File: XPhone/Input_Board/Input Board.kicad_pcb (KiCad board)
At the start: 2 copper layers, 92 parts, among them J1 AUDIO, J10 ENV, J11 PULSE, J12 PULSE, J2 AUDIO, J3 ENV, J4 ENV, J5 PULSE, J6 PULSE, J7 AUDIO, J8 AUDIO, J9 ENV, Q1 BC847CW, Q2 BC847CW, Q3 BC847CW, Q4 BC847CW, Q5 BC847CW, Q6 BC847CW, Q7 BC847CW, Q8 BC847CW, U1 LM833, U2 78L05, U3 TL084, U4 74HC14, U5 LM833

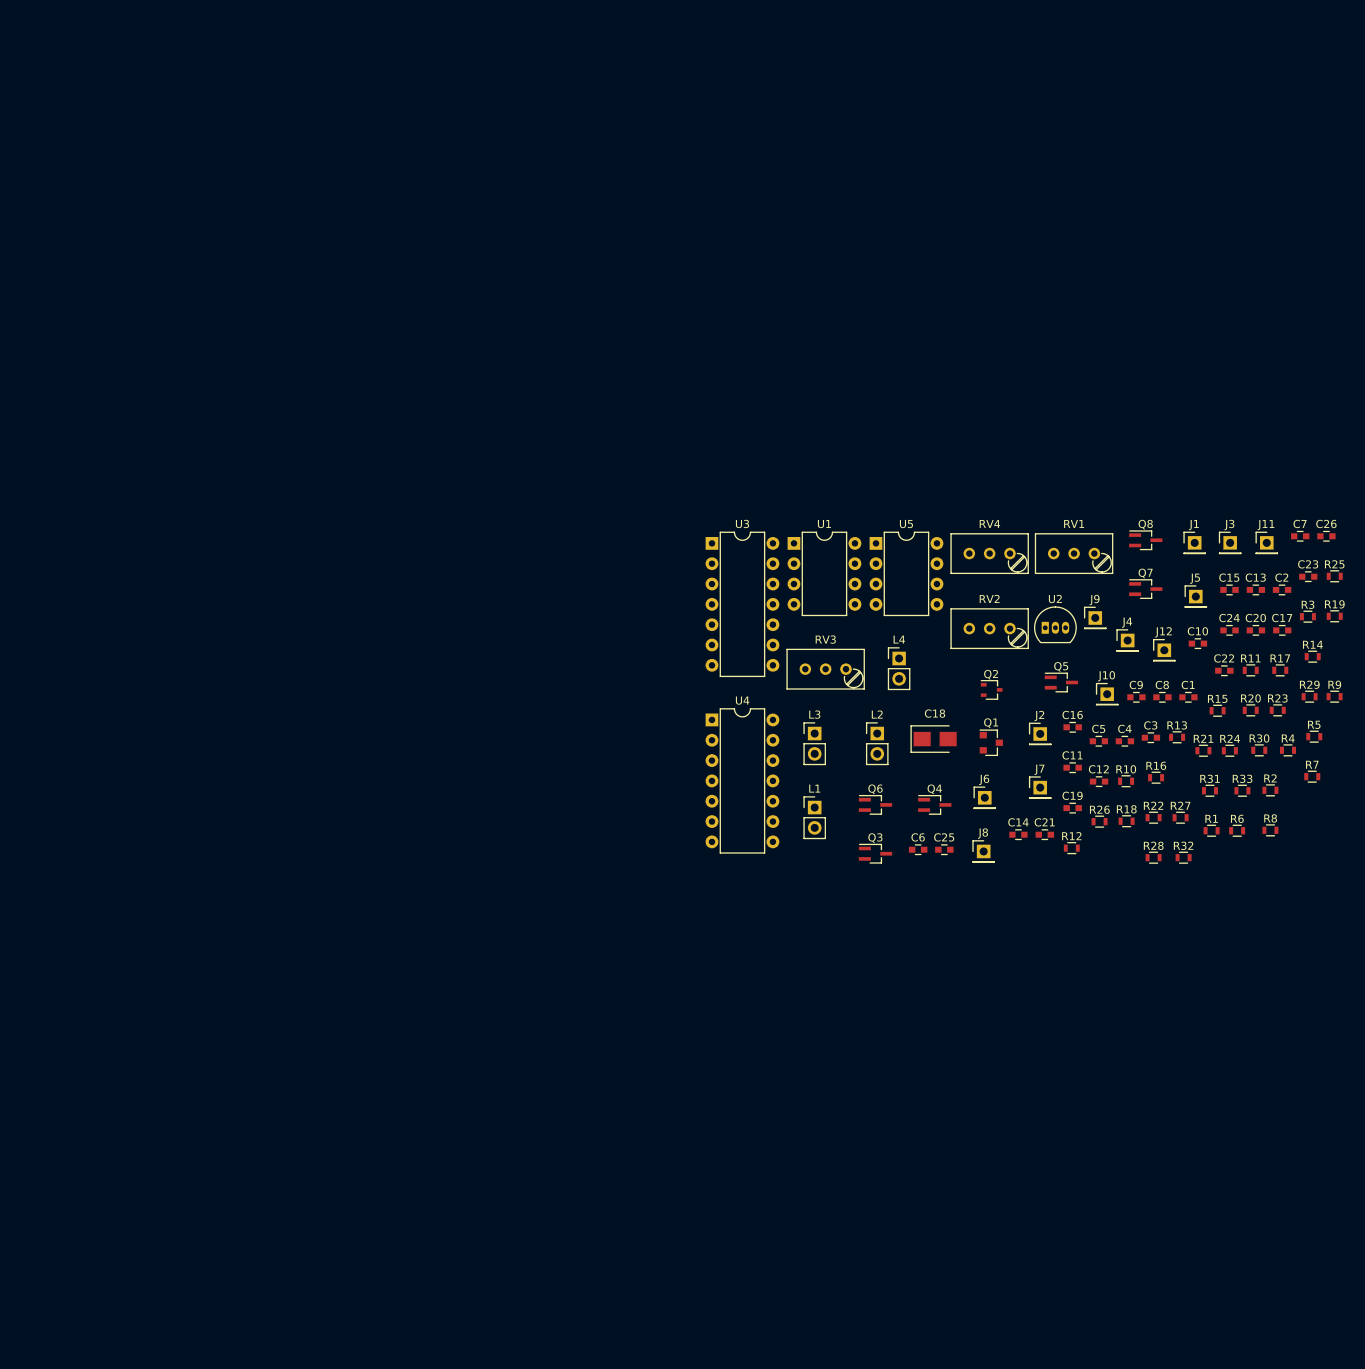
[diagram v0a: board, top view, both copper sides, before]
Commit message: ^XPhone Input Board layout; +bug record
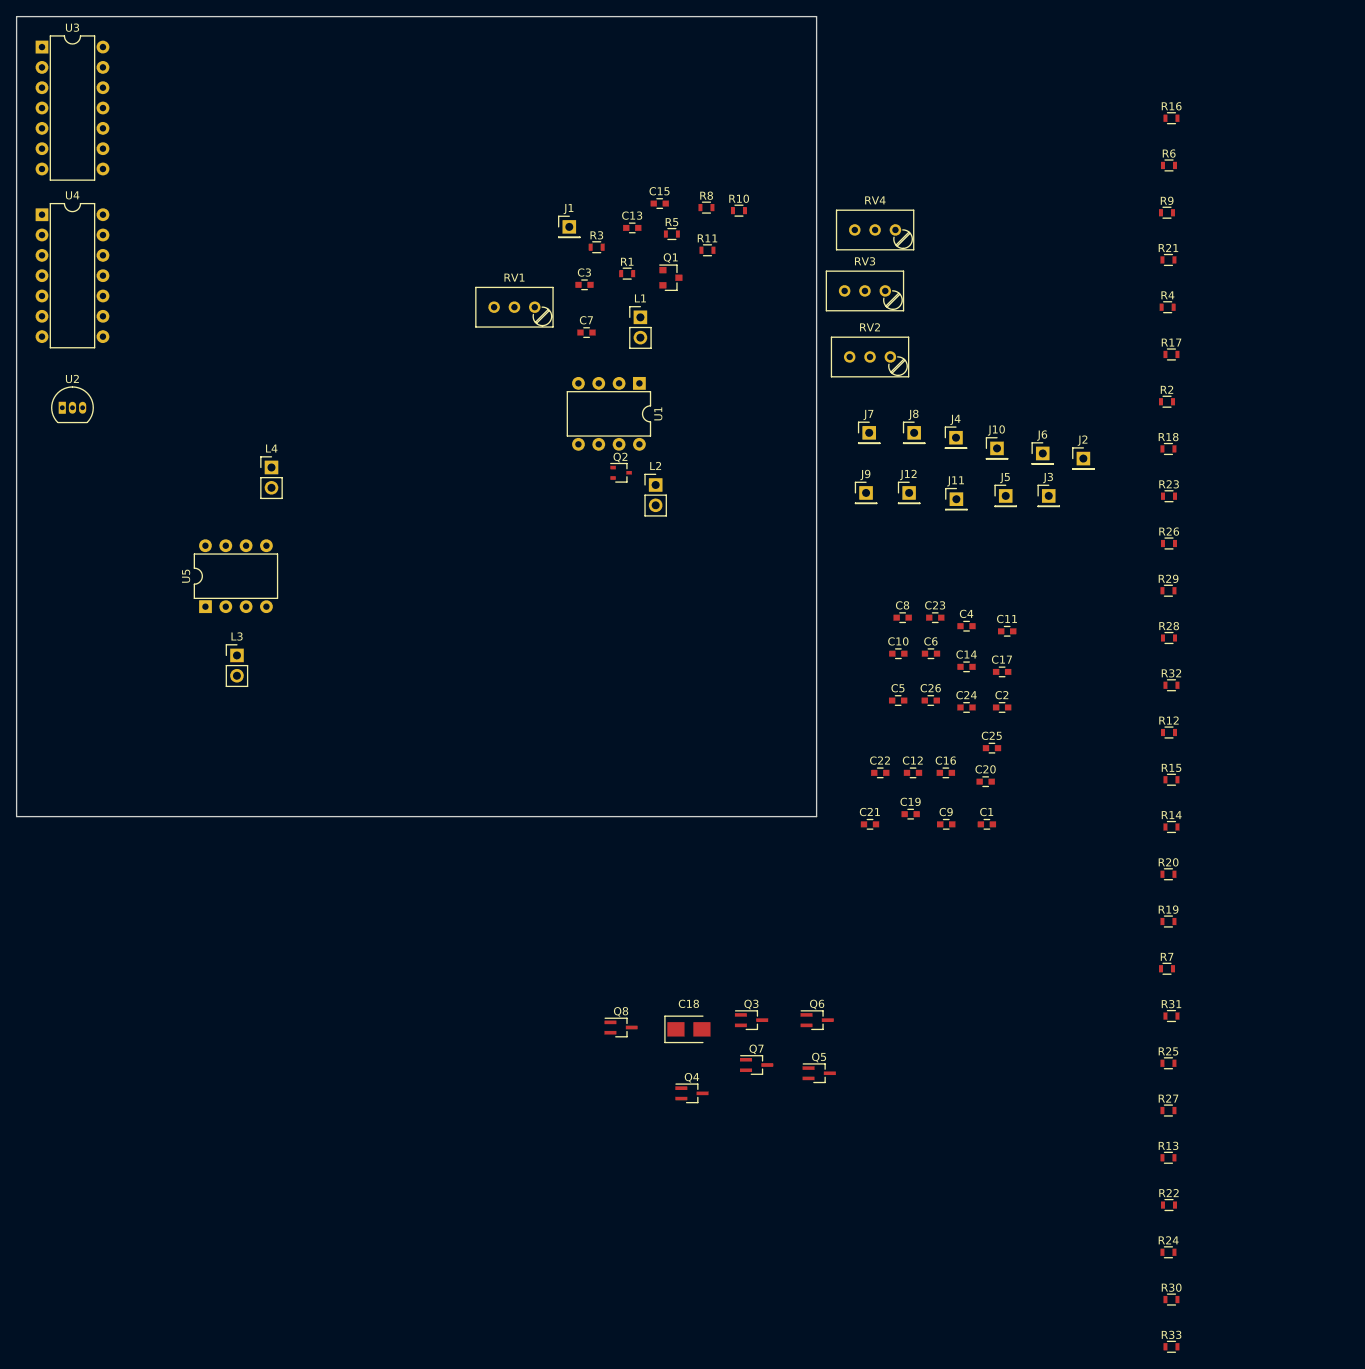
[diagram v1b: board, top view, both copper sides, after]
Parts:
- moved U2 125.9 mm to (5.71, 48.9)
- moved R8 105.0 mm to (86.2, 23.9)
- moved U4 104.9 mm to (3.17, 24.8)
- moved U3 104.2 mm to (3.17, 3.81)
- moved R5 101.9 mm to (81.9, 27.2)
- moved R1 100.9 mm to (76.3, 32.1)
- moved R3 100.2 mm to (72.5, 28.8)
- moved C7 92.8 mm to (71.2, 39.5)
- moved C3 90.6 mm to (71.0, 33.5)
- moved C13 90.1 mm to (77.0, 26.4)
- moved Q8 89.5 mm to (75.6, 126.4)
- moved J1 87.6 mm to (69.1, 26.3)
- moved R10 86.2 mm to (90.3, 24.3)
- moved C15 86.1 mm to (80.4, 23.4)
- moved R11 85.8 mm to (86.4, 29.2)
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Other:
- board outline added: 100 x 100 mm
- net class Default: clearance 0.2 -> 0.3; trace_width 0.25 -> 0.3; via_dia 0.6 -> 1; via_drill 0.4 -> 0.6
- net class Power added: clearance 0.6, trace_width 1, via_dia 1, via_drill 0.6
- rule trace_clearance: 0.2 -> 0.3

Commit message: XPhone/Input_Board components are roughly organized
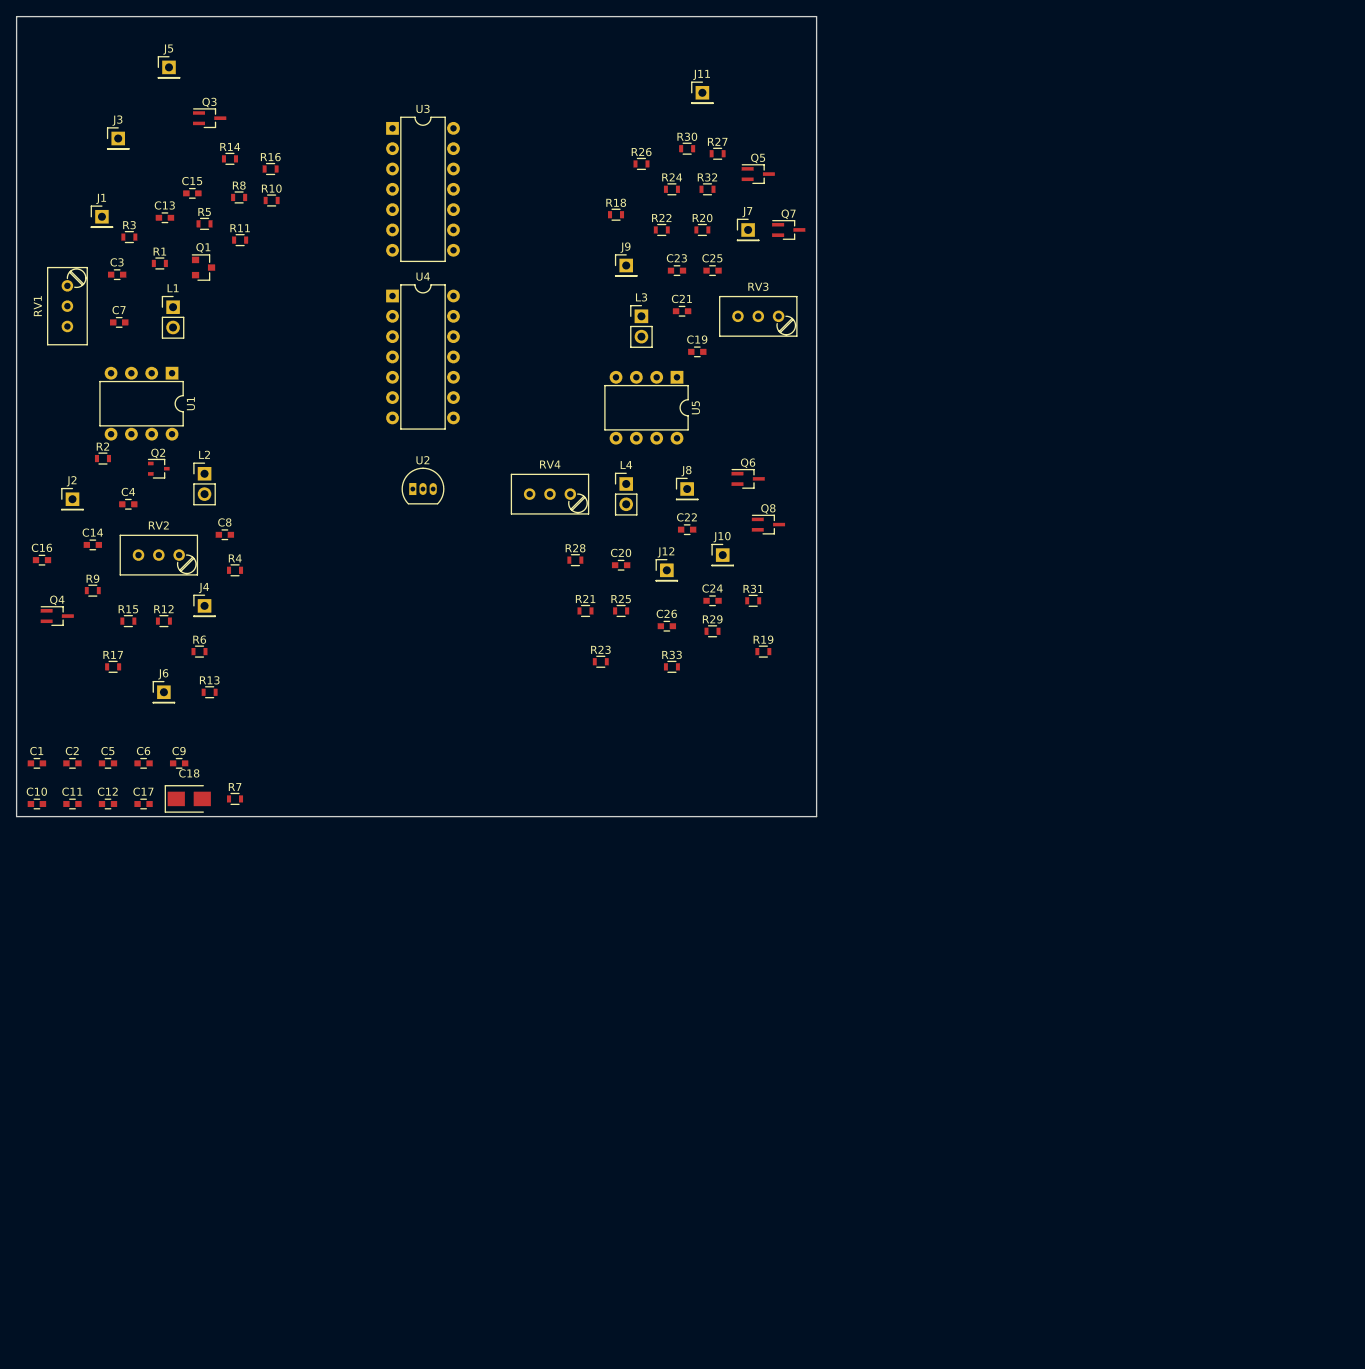
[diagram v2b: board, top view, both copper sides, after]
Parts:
- moved R30 156.1 mm to (83.8, 16.5)
- moved R24 146.7 mm to (81.9, 21.6)
- moved R14 144.3 mm to (26.7, 17.8)
- moved R9 142.3 mm to (9.53, 71.8)
- moved R17 137.9 mm to (12.1, 81.3)
- moved R22 137.4 mm to (80.6, 26.7)
- moved R6 135.6 mm to (22.9, 79.4)
- moved R13 133.2 mm to (24.1, 84.5)
- moved R2 133.2 mm to (10.8, 55.2)
- moved R27 132.2 mm to (87.6, 17.1)
- moved R15 131.9 mm to (14.0, 75.6)
- moved Q3 131.5 mm to (24.1, 12.7)
- moved J2 126.5 mm to (6.99, 60.3)
- moved R12 126.4 mm to (18.4, 75.6)
- moved J3 124.6 mm to (12.7, 15.2)
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
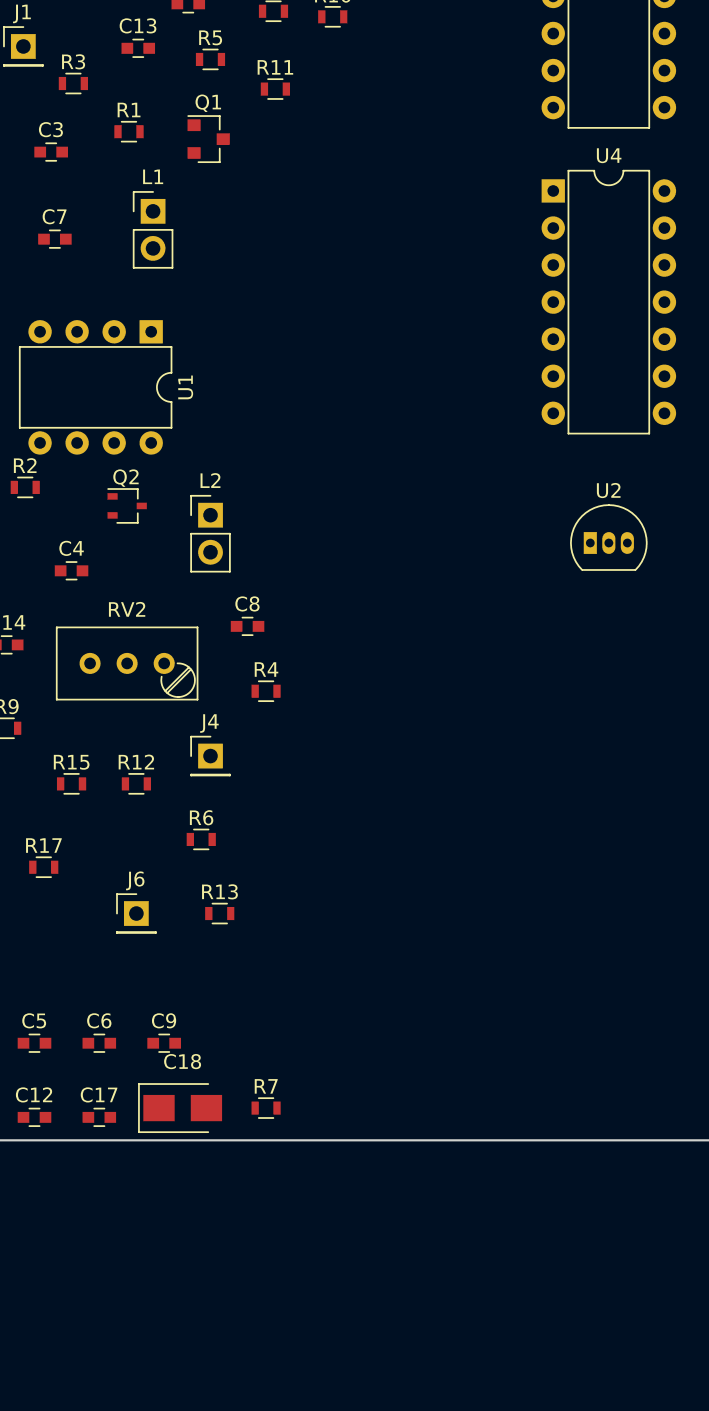
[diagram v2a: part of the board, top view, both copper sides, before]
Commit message: XPhone/Input_Board +power connectors
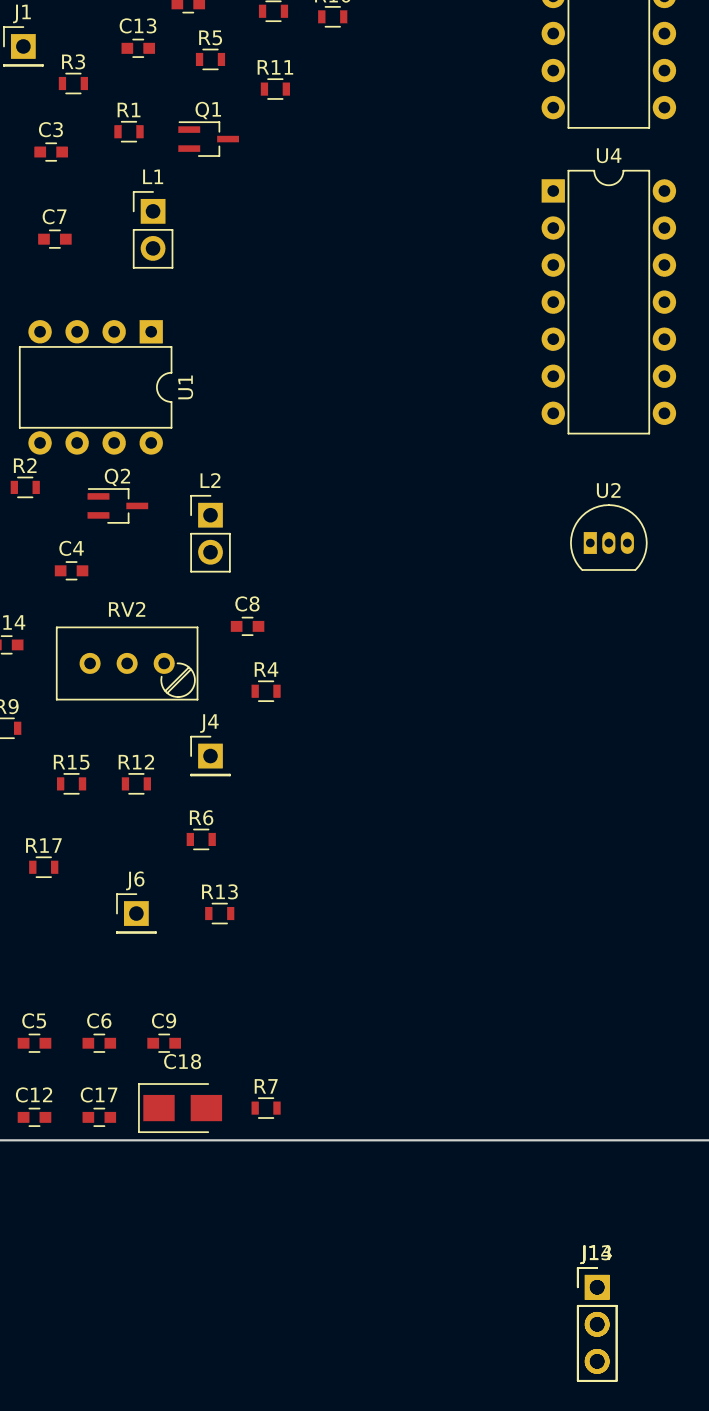
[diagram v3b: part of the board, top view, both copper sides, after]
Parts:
- added J13: Power In, Pin_Headers:Pin_Header_Straight_1x03_Pitch2.54mm, F.Cu at (50.0, 110.1)
- added J14: Power Out, Pin_Headers:Pin_Header_Straight_1x03_Pitch2.54mm, F.Cu at (50.0, 110.1)
- Q1: footprint TO_SOT_Packages_SMD:SOT-23 -> TO_SOT_Packages_SMD:SOT-323_SC-70_Handsoldering
- Q2: footprint TO_SOT_Packages_SMD:SOT-323_SC-70 -> TO_SOT_Packages_SMD:SOT-323_SC-70_Handsoldering
- moved Q2 0.64 mm to (17.1, 56.5)
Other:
- net class Power: clearance 0.6 -> 0.5

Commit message: ^XPhone/Input_Board
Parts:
- moved J13 24.7 mm to (32.4, 92.7)
- moved J14 23.0 mm to (34.9, 92.7)
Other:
- net class Power: trace_width 1 -> 0.8
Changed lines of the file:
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@@
   (general
     (links 174)
-    (no_connects 171)
-    (area -0.075001 -0.075001 100.075001 100.075001)
+    (no_connects 174)
+    (area -0.075001 -0.075001 100.52 102.315)
     (thickness 1.6)
     (drawings 4)
@@
   (net_class Power ""
     (clearance 0.5)
-    (trace_width 1)
+    (trace_width 0.8)
     (via_dia 1)
     (via_drill 0.6)
@@
   )
   (module Pin_Headers:Pin_Header_Straight_1x03_Pitch2.54mm (layer F.Cu)
-    (at 50 110.075001)
+    (at 32.385 92.71)
     (descr "Through hole straight pin header, 1x03, 2.54mm pitch, single row")
     (tags "Through hole pin header THT 1x03 2.54mm single row")
-    (fp_text reference J13 (at 0 -2.33) (layer F.SilkS)
+    (fp_text reference J13 (at -0.635 -2.54) (layer F.SilkS)
       (effects (font (size 1 1) (thickness 0.15)))
     )
-    (fp_text value "Power In" (at 0 7.41) (layer F.Fab)
+    (fp_text value "Power In" (at -2.54 2.54 90) (layer F.Fab)
       (effects (font (size 1 1) (thickness 0.15)))
     )
@@
     (fp_line (start 1.8 6.85) (end 1.8 -1.8) (layer F.CrtYd) (width 0.05))
     (fp_line (start 1.8 -1.8) (end -1.8 -1.8) (layer F.CrtYd) (width 0.05))
-    (fp_text user %R (at 0 -2.33) (layer F.Fab)
+    (fp_text user %R (at -0.635 -2.54) (layer F.Fab)
       (effects (font (size 1 1) (thickness 0.15)))
     )
@@
   )
   (module Pin_Headers:Pin_Header_Straight_1x03_Pitch2.54mm (layer F.Cu)
-    (at 50 110.075001)
+    (at 34.925 92.71)
     (descr "Through hole straight pin header, 1x03, 2.54mm pitch, single row")
     (tags "Through hole pin header THT 1x03 2.54mm single row")
-    (fp_text reference J14 (at 0 -2.33) (layer F.SilkS)
+    (fp_text reference J14 (at 0.635 -2.54) (layer F.SilkS)
       (effects (font (size 1 1) (thickness 0.15)))
     )
-    (fp_text value "Power Out" (at 0 7.41) (layer F.Fab)
+    (fp_text value "Power Out" (at 2.54 2.54 90) (layer F.Fab)
       (effects (font (size 1 1) (thickness 0.15)))
     )
@@
     (fp_line (start 1.8 6.85) (end 1.8 -1.8) (layer F.CrtYd) (width 0.05))
     (fp_line (start 1.8 -1.8) (end -1.8 -1.8) (layer F.CrtYd) (width 0.05))
-    (fp_text user %R (at 0 -2.33) (layer F.Fab)
+    (fp_text user %R (at 0.635 -2.54) (layer F.Fab)
       (effects (font (size 1 1) (thickness 0.15)))
     )

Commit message: XPhone/Input_Board
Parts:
- C1, C10, C11, C12, C13, C14, C15, C16, C17, C19, C2, C20, C21, C22, C23, C24, C25, C26, C3, C4, C5, C6, C7, C8, C9: footprint Capacitors_SMD:C_0603 -> Capacitors_SMD:C_0603_HandSoldering
- R1, R10, R11, R12, R13, R14, R15, R16, R17, R18, R19, R2, R20, R21, R22, R23, R24, R25, R26, R27, R28, R29, R3, R30, R31, R32, R33, R4, R5, R6, R7, R8, R9: footprint Resistors_SMD:R_0603 -> Resistors_SMD:R_0603_HandSoldering
- U4: footprint Housings_DIP:DIP-14_W7.62mm -> SMD_Packages:SOIC-14_N
- moved R2 15.3 mm to (21.6, 66.0)
- moved C1 15.3 mm to (13.3, 104.1)
- moved C10 15.3 mm to (13.3, 109.2)
- moved C11 15.3 mm to (17.8, 109.2)
- moved C12 15.3 mm to (22.2, 109.2)
- moved C16 15.3 mm to (14.0, 78.7)
- moved C17 15.3 mm to (26.7, 109.2)
- moved C19 15.3 mm to (95.9, 52.7)
- moved C2 15.3 mm to (17.8, 104.1)
- moved C20 15.3 mm to (86.4, 79.4)
- moved C21 15.3 mm to (94.0, 47.6)
- moved C22 15.3 mm to (94.6, 74.9)
- moved C23 15.3 mm to (93.3, 42.5)
- moved C25 15.3 mm to (97.8, 42.5)
- moved C26 15.3 mm to (92.1, 87.0)
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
